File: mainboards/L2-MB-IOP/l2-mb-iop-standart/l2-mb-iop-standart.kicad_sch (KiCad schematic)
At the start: 43 parts, among them J1 Conn_01x03_Pin, J10 Conn_01x01_Pin, J11 Conn_01x01_Pin, J12 Conn_01x01_Pin, J13 Conn_01x01_Pin, J14 URP_Conn_01x12_Socket, J15 URP_Conn_01x12_Socket, J16 GPP_Conn_01x12_Socket, J17 GPP_Conn_01x12_Socket, J18 GPP_Conn_01x12_Socket, J19 GPP_Conn_01x12_Socket, J2 Conn_01x01_Pin, J20 GPP_Conn_01x12_Socket, J21 GPP_Conn_01x12_Socket, J22 GPP_Conn_01x12_Socket, J23 GPP_Conn_01x12_Socket, J24 GPP_Conn_01x12_Socket, J25 GPP_Conn_01x12_Socket, J26 GPP_Conn_01x12_Socket, J27 GPP_Conn_01x12_Socket, J28 AIP_Conn_01x12_Socket, J29 AIP_Conn_01x12_Socket, J3 Conn_01x01_Pin, J30 AIP_Conn_01x12_Socket, J31 AIP_Conn_01x12_Socket, J32 ICP_Conn_01x12_Socket, J33 ICP_Conn_01x12_Socket, J34 AIP_Conn_01x12_Socket, J35 AIP_Conn_01x12_Socket, J4 Conn_01x01_Pin, J5 Conn_01x01_Pin, J6 Conn_01x01_Pin, J7 Conn_01x01_Pin, J8 Conn_01x01_Pin, J9 Conn_01x01_Pin

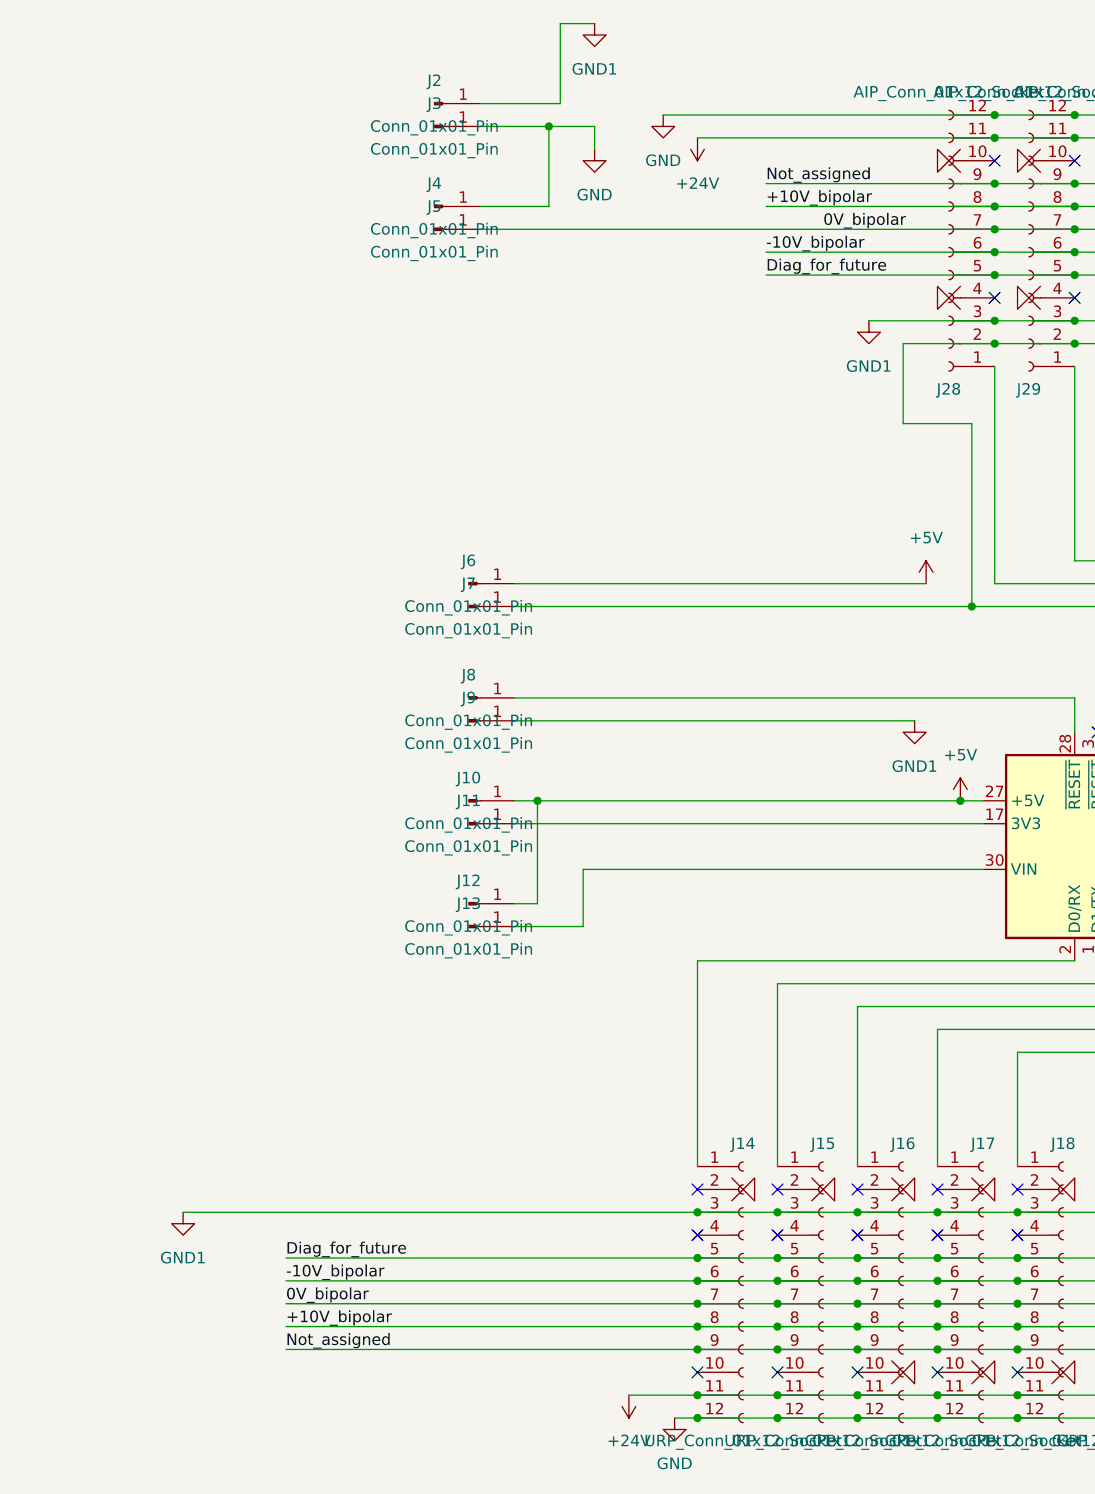
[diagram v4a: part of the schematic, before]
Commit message: Created DIO board.
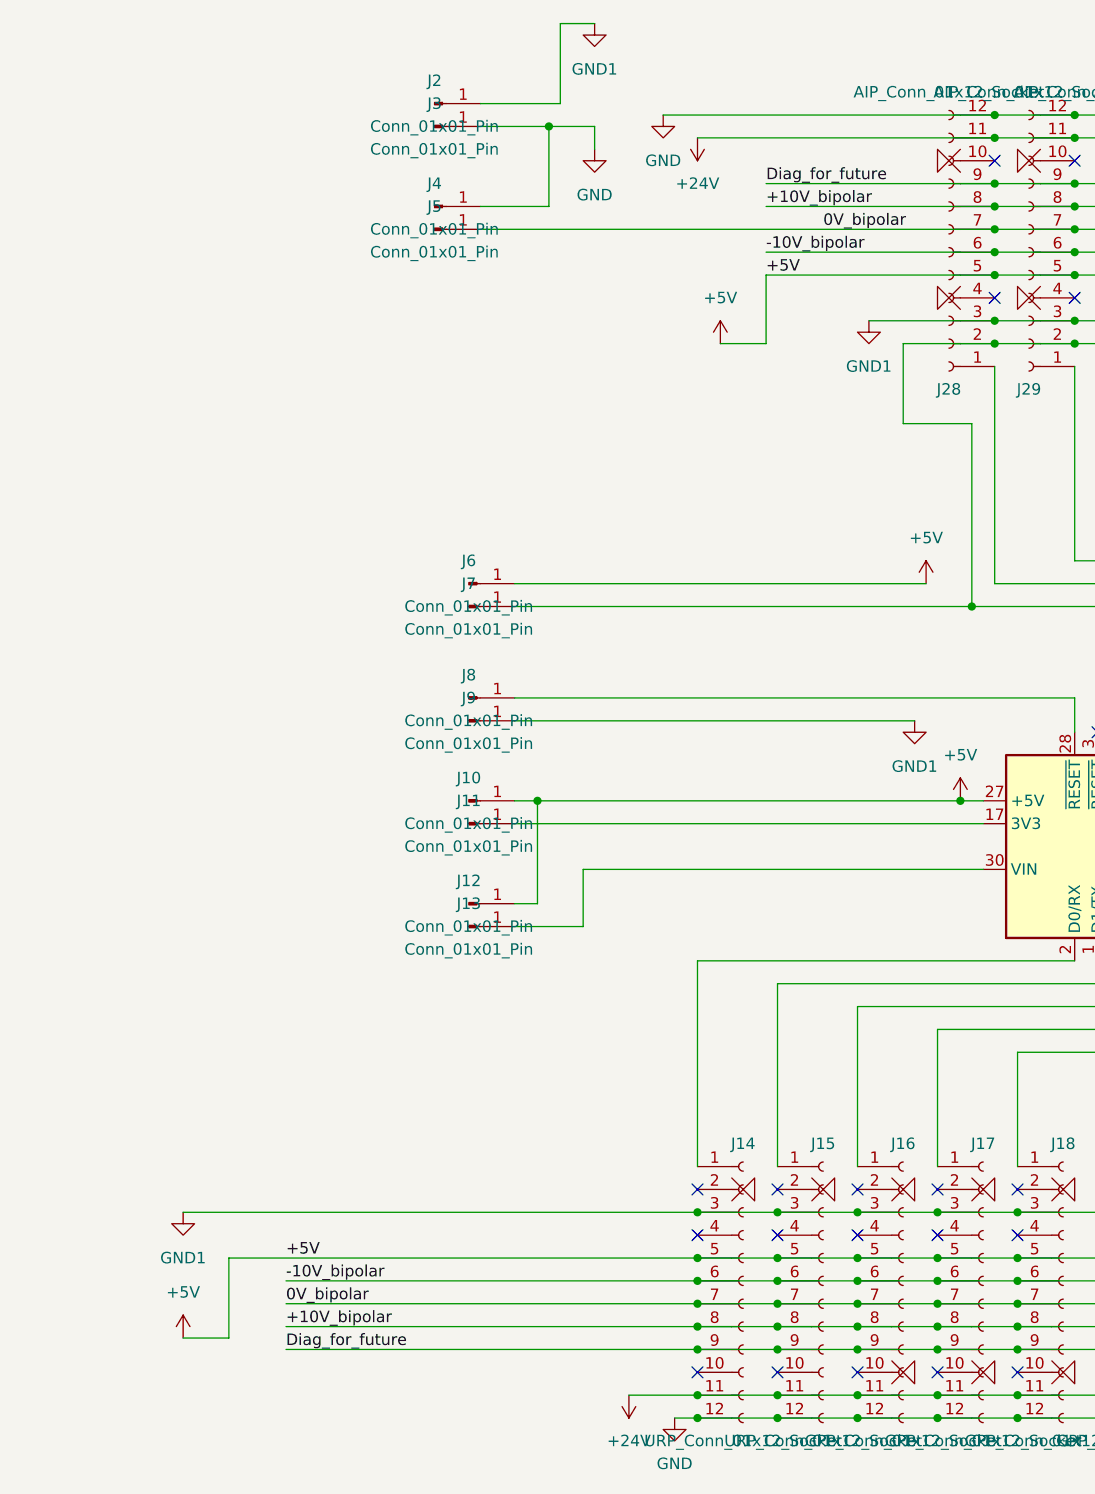
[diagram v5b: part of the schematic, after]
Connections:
- net Not_assigned is gone; now on net Diag_for_future: J14.9 (N/A_Pin_9), J15.9 (N/A_Pin_9), J16.9 (N/A_Pin_9), J17.9 (N/A_Pin_9), J18.9 (N/A_Pin_9), J19.9 (N/A_Pin_9), J20.9 (N/A_Pin_9), J21.9 (N/A_Pin_9), J22.9 (N/A_Pin_9), J23.9 (N/A_Pin_9), J24.9 (N/A_Pin_9), J25.9 (N/A_Pin_9), J26.9 (N/A_Pin_9), J27.9 (N/A_Pin_9), J28.9 (N/A_Pin_9), J29.9 (N/A_Pin_9), J30.9 (N/A_Pin_9), J31.9 (N/A_Pin_9), J32.9 (N/A_Pin_9), J33.9 (N/A_Pin_9), J34.9 (N/A_Pin_9), J35.9 (N/A_Pin_9)
- net +5V: now also J14.5 (Diag), J15.5 (Diag), J16.5 (Diag), J17.5 (Diag), J18.5 (Diag), J19.5 (Diag), J20.5 (Diag), J21.5 (Diag), J22.5 (Diag), J23.5 (Diag), J24.5 (Diag), J25.5 (Diag), J26.5 (Diag), J27.5 (Diag), J28.5 (Diag), J29.5 (Diag), J30.5 (Diag), J31.5 (Diag), J32.5 (Diag), J33.5 (Diag), J34.5 (Diag), J35.5 (Diag)
- net Diag_for_future: no longer J14.5 (Diag), J15.5 (Diag), J16.5 (Diag), J17.5 (Diag), J18.5 (Diag), J19.5 (Diag), J20.5 (Diag), J21.5 (Diag), J22.5 (Diag), J23.5 (Diag), J24.5 (Diag), J25.5 (Diag), J26.5 (Diag), J27.5 (Diag), J28.5 (Diag), J29.5 (Diag), J30.5 (Diag), J31.5 (Diag), J32.5 (Diag), J33.5 (Diag), J34.5 (Diag), J35.5 (Diag)
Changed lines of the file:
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@@
 	(wire
 		(pts
+			(xy 168.91 201.93) (xy 163.83 201.93)
+		)
+		(stroke
+			(width 0)
+			(type default)
+		)
+	)
+	(wire
+		(pts
 			(xy 220.98 210.82) (xy 229.87 210.82)
 		)
@@
 	(wire
 		(pts
+			(xy 168.91 193.04) (xy 168.91 201.93)
+		)
+		(stroke
+			(width 0)
+			(type default)
+		)
+	)
+	(wire
+		(pts
 			(xy 220.98 200.66) (xy 229.87 200.66)
 		)
@@
 	(wire
 		(pts
-			(xy 175.26 193.04) (xy 220.98 193.04)
-		)
-		(stroke
-			(width 0)
-			(type default)
-		)
-	)
-	(wire
-		(pts
 			(xy 238.76 193.04) (xy 247.65 193.04)
 		)
@@
 	(wire
 		(pts
+			(xy 168.91 193.04) (xy 220.98 193.04)
+		)
+		(stroke
+			(width 0)
+			(type default)
+		)
+	)
+	(wire
+		(pts
 			(xy 289.56 83.82) (xy 298.45 83.82)
 		)
@@
 	(wire
 		(pts
+			(xy 228.6 83.82) (xy 228.6 91.44)
+		)
+		(stroke
+			(width 0)
+			(type default)
+		)
+	)
+	(wire
+		(pts
 			(xy 312.42 195.58) (xy 321.31 195.58)
 		)
@@
 	(wire
 		(pts
+			(xy 228.6 91.44) (xy 223.52 91.44)
+		)
+		(stroke
+			(width 0)
+			(type default)
+		)
+	)
+	(wire
+		(pts
 			(xy 298.45 115.57) (xy 298.45 93.98)
 		)
@@
 		)
 	)
-	(label "Diag_for_future"
+	(label "+5V"
 		(at 228.6 83.82 0)
 		(effects
@@
 		)
 	)
-	(label "Diag_for_future"
+	(label "+5V"
 		(at 175.26 193.04 0)
 		(effects
@@
 		)
 	)
-	(label "Not_assigned"
+	(label "Diag_for_future"
 		(at 228.6 73.66 0)
 		(effects
@@
 		)
 	)
-	(label "Not_assigned"
+	(label "Diag_for_future"
 		(at 175.26 203.2 0)
 		(effects
@@
 	)
 	(symbol
+		(lib_id "power:+5V")
+		(at 163.83 201.93 0)
+		(unit 1)
+		(exclude_from_sim no)
+		(in_bom yes)
+		(on_board yes)
+		(dnp no)
+		(fields_autoplaced yes)
+		(property "Reference" "#PWR024"
+			(at 163.83 205.74 0)
+			(effects
+				(font
+					(size 1.27 1.27)
+				)
+				(hide yes)
+			)
+		)
+		(property "Value" "+5V"
+			(at 163.83 196.85 0)
+			(effects
+				(font
+					(size 1.27 1.27)
+				)
+			)
+		)
+		(property "Footprint" ""
+			(at 163.83 201.93 0)
+			(effects
+				(font
+					(size 1.27 1.27)
+				)
+				(hide yes)
+			)
+		)
+		(property "Datasheet" ""
+			(at 163.83 201.93 0)
+			(effects
+				(font
+					(size 1.27 1.27)
+				)
+				(hide yes)
+			)
+		)
+		(property "Description" "Power symbol creates a global label with name \"+5V\""
+			(at 163.83 201.93 0)
+			(effects
+				(font
+					(size 1.27 1.27)
+				)
+				(hide yes)
+			)
+		)
+		(pin "1"
+		)
+		(instances
+			(project "l2-mb-iop-standart"
+				(path "/f25cfa12-e490-4a92-ab8c-1b3ce123d4e0"
+					(reference "#PWR024")
+					(unit 1)
+				)
+			)
+		)
+	)
+	(symbol
 		(lib_id "power:+24V")
 		(at 27.94 106.68 0)
@@
 					(unit 1)
 				)
+			)
+		)
+	)
+	(symbol
+		(lib_id "power:+5V")
+		(at 223.52 91.44 0)
+		(unit 1)
+		(exclude_from_sim no)
+		(in_bom yes)
+		(on_board yes)
+		(dnp no)
+		(fields_autoplaced yes)
+		(property "Reference" "#PWR023"
+			(at 223.52 95.25 0)
+			(effects
+				(font
+					(size 1.27 1.27)
+				)
+				(hide yes)
+			)
+		)
+		(property "Value" "+5V"
+			(at 223.52 86.36 0)
+			(effects
+				(font
+					(size 1.27 1.27)
+				)
+			)
+		)
+		(property "Footprint" ""
+			(at 223.52 91.44 0)
+			(effects
+				(font
+					(size 1.27 1.27)
+				)
+				(hide yes)
+			)
+		)
+		(property "Datasheet" ""
+			(at 223.52 91.44 0)
+			(effects
+				(font
+					(size 1.27 1.27)
+				)
+				(hide yes)
+			)
+		)
+		(property "Description" "Power symbol creates a global label with name \"+5V\""
+			(at 223.52 91.44 0)
+			(effects
+				(font
+					(size 1.27 1.27)
+				)
+				(hide yes)
+			)
+		)
+		(pin "1"
+		)
+		(instances
+			(project "l2-mb-iop-standart"
+				(path "/f25cfa12-e490-4a92-ab8c-1b3ce123d4e0"
+					(reference "#PWR023")
+					(unit 1)
+				)
